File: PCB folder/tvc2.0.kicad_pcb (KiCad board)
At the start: 4 copper layers, 95 x 54 mm, 15 parts, among them U1 Teensy4.1, U5 LM7805_TO220

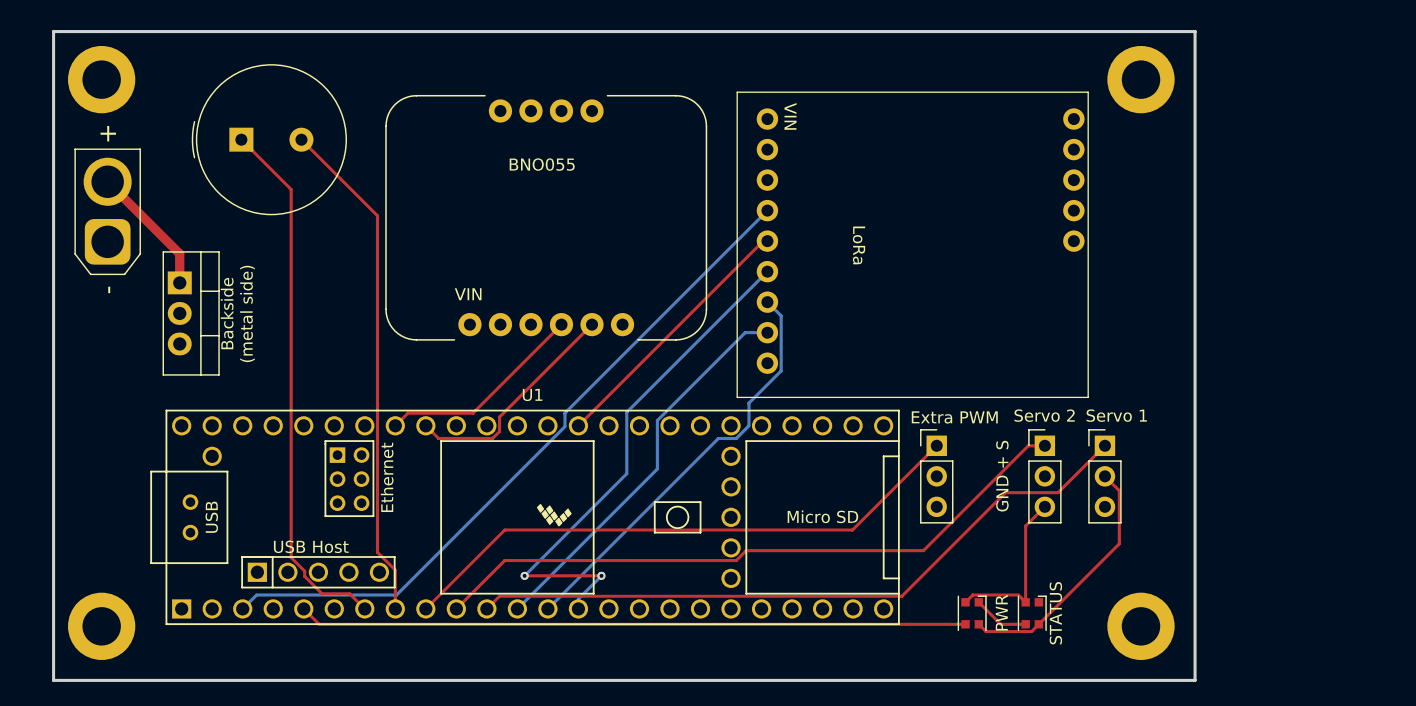
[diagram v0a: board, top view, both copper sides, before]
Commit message: funts: Added Pyro circuit in schematic
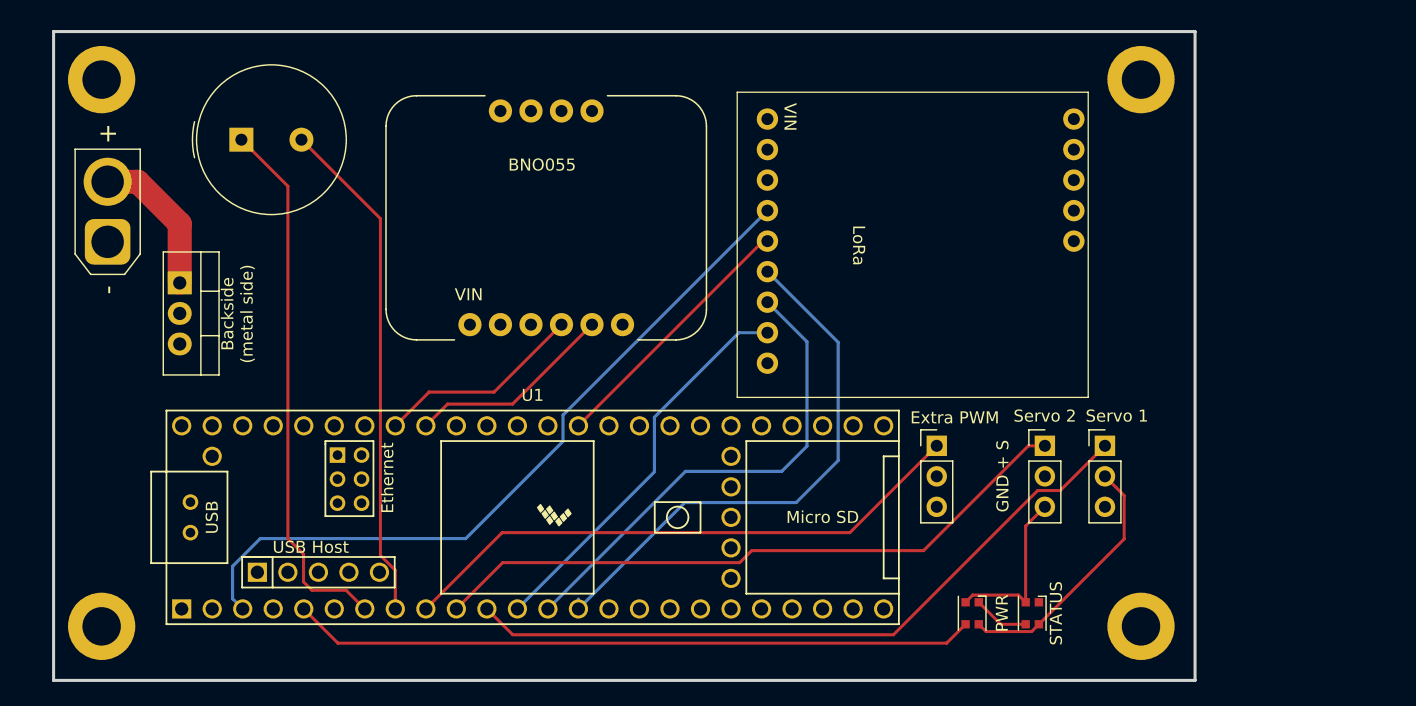
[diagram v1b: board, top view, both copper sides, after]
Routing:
- net /11_MOSI_CTX1: track 34.9 -> 40.5 mm
- net /1_TX1_CTX2_MISO1: track 58.1 -> 62.2 mm
- net /12_MISO_MQSL: track 43.6 -> 45.7 mm, vias 2 -> 0
- net /9_OUT1C: track 57.1 -> 58.8 mm
- net /18_A4_SDA: track 18.9 -> 17.3 mm
- net +7.5V: track 10.9 -> 12.4 mm
- net /3_LRCLK2: track 55.6 -> 56.9 mm

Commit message: functs: update PCB, add part excel
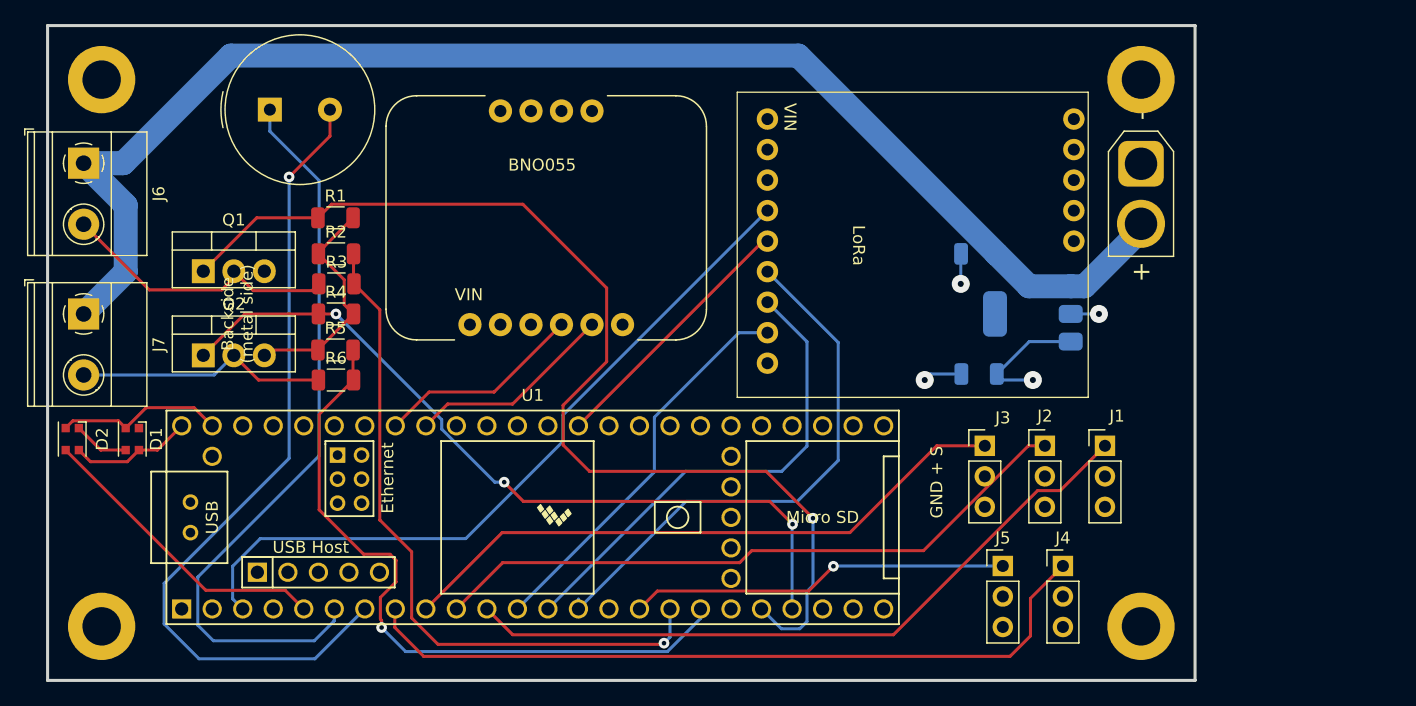
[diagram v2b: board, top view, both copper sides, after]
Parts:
- added C1: 0.33uf, Capacitor_SMD:C_1206_3216Metric, B.Cu at (202.5, 37.0)
- added C2: 0.1uf, Capacitor_SMD:C_1206_3216Metric, B.Cu at (202.5, 47.0)
- added J4: PWM Test OUT, Connector_PinHeader_2.54mm:PinHeader_1x03_P2.54mm_Vertical, F.Cu at (209.5, 63.0)
- added J5: PWM Test OUT, Connector_PinHeader_2.54mm:PinHeader_1x03_P2.54mm_Vertical, F.Cu at (204.5, 63.0)
- added J6: Screw_Terminal_01x02, TerminalBlock_Phoenix:TerminalBlock_Phoenix_MKDS-1,5-2-5.08_1x02_P5.08mm_Horizontal, F.Cu at (128.0, 29.5)
- added J7: Screw_Terminal_01x02, TerminalBlock_Phoenix:TerminalBlock_Phoenix_MKDS-1,5-2-5.08_1x02_P5.08mm_Horizontal, F.Cu at (128.0, 42.0)
- added Q1: IRLZ44NPBF, Package_TO_SOT_THT:TO-220-3_Vertical, F.Cu at (138.0, 38.4)
- added Q2: IRLZ44NPBF, Package_TO_SOT_THT:TO-220-3_Vertical, F.Cu at (138.0, 45.4)
- added R1: 1k, Resistor_SMD:R_1206_3216Metric, F.Cu at (149.0, 34.0)
- added R2: 51k, Resistor_SMD:R_1206_3216Metric, F.Cu at (149.0, 37.0)
- added R3: 91k, Resistor_SMD:R_1206_3216Metric, F.Cu at (149.0, 39.5)
- added R4: 1k, Resistor_SMD:R_1206_3216Metric, F.Cu at (149.0, 42.0)
- added R5: 51k, Resistor_SMD:R_1206_3216Metric, F.Cu at (149.0, 45.0)
- added R6: 91k, Resistor_SMD:R_1206_3216Metric, F.Cu at (149.0, 47.5)
- J1: renamed from Servo 1
- J2: renamed from Servo 2
- J3: renamed from Extra PWM
- U1: footprint Teensy4.1:Teensy41 -> tvc499:Teensy41
- U2: footprint LoRa_RF95:LoRa_RF95 Breakout -> tvc499:LoRa_RF95 Breakout
- U3: footprint BNO055:BNO055 -> tvc499:BNO055
- U5: footprint Package_TO_SOT_THT:TO-220-3_Vertical -> Package_TO_SOT_SMD:SOT-223; moved to B.Cu
- moved REF** 86.2 mm to (216.0, 29.5), turned to -90 degrees
- moved D2 76.3 mm to (127.0, 52.4)
- moved D1 76.3 mm to (132.1, 52.4)
- moved U5 71.0 mm to (207.0, 42.0), turned to 180 degrees
- moved J3 4.00 mm to (203.0, 53.0)
- moved BZ1 3.45 mm to (143.5, 25.0)
- renumbered STATUS to D1, PWR to D2
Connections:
- BZ1 pad 1: /5_IN2 -> /4_BCLK2
- BZ1 pad 2: /6_OUT1D -> /5_IN2
- U1 pad 46: (no net) -> +3.3V
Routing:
- net +7.5V: track 12.4 -> 117.6 mm
- net /28_RX7: track 0.00 -> 90.2 mm, vias 0 -> 1
- net /29_TX7: track 0.00 -> 65.2 mm, vias 0 -> 3
- net /4_BCLK2: track 0.00 -> 62.4 mm
- net /26_A12_MOSI1: track 0.00 -> 58.6 mm, vias 0 -> 1
- net /25_A11_RX6_SDA2: track 0.00 -> 57.3 mm, vias 0 -> 1
- net /24_A10_TX6_SCL2: track 0.00 -> 31.7 mm, vias 0 -> 1
- net /3_LRCLK2: track 56.9 -> 25.3 mm
- net GND: track 14.1 -> 41.4 mm, vias 0 -> 3
- net Net-(J6-Pin_2): track 0.00 -> 23.7 mm
- net /5_IN2: track 45.0 -> 68.6 mm, vias 0 -> 1
- net Net-(J7-Pin_2): track 0.00 -> 21.1 mm
- net /6_OUT1D: track 42.3 -> 63.1 mm
- net /7_RX2_OUT1A: track 48.1 -> 52.1 mm
- net +5V: track 21.4 -> 20.7 mm, vias 0 -> 1
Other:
- board size 95 x 54 mm -> 95.5 x 54.5 mm

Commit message: added pcb name date version
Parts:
- PWM 24: renamed from J5
- PWM 6: renamed from J4
- PWM 7: renamed from J3
- PWM 8: renamed from J2
- PWM 9: renamed from J1
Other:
- board text added: "C3C GRANT STEC TVC499 Flight Computer v1 11/20/24"
- board text added: "SERVO"
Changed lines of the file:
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@@
 		(descr "Through hole straight pin header, 1x03, 2.54mm pitch, single row")
 		(tags "Through hole pin header THT 1x03 2.54mm single row")
-		(property "Reference" "J3"
-			(at 1.5 -2.33 0)
+		(property "Reference" "PWM 7"
+			(at -0.8 -2.475 0)
 			(layer "F.SilkS")
 			(effects
@@
 		(descr "Through hole straight pin header, 1x03, 2.54mm pitch, single row")
 		(tags "Through hole pin header THT 1x03 2.54mm single row")
-		(property "Reference" "J2"
+		(property "Reference" "PWM 8"
 			(at 0 -2.475 0)
 			(layer "F.SilkS")
@@
 		(descr "Through hole straight pin header, 1x03, 2.54mm pitch, single row")
 		(tags "Through hole pin header THT 1x03 2.54mm single row")
-		(property "Reference" "J4"
-			(at 0 -2.33 0)
+		(property "Reference" "PWM 6"
+			(at 0.6 -2.375 0)
 			(layer "F.SilkS")
 			(effects
@@
 		(descr "Through hole straight pin header, 1x03, 2.54mm pitch, single row")
 		(tags "Through hole pin header THT 1x03 2.54mm single row")
-		(property "Reference" "J1"
-			(at 1 -2.475 0)
+		(property "Reference" "PWM 9"
+			(at 0.7 -2.475 0)
 			(layer "F.SilkS")
 			(effects
@@
 		(descr "Through hole straight pin header, 1x03, 2.54mm pitch, single row")
 		(tags "Through hole pin header THT 1x03 2.54mm single row")
-		(property "Reference" "J5"
+		(property "Reference" "PWM 24"
 			(at 0 -2.33 0)
 			(layer "F.SilkS")
@@
 		(property "Value" "PWM Test OUT"
 			(at 0 7.41 0)
-			(layer "F.Fab")
+			(layer "F.SilkS")
 			(effects
 				(font
@@
 	)
 	(gr_text "GND + S\n"
+		(at 200.7 65.6 90)
+		(layer "F.SilkS")
+		(effects
+			(font
+				(size 1 1)
+				(thickness 0.15)
+			)
+		)
+	)
+	(gr_text "SERVO\n"
+		(at 216 55.4 90)
+		(layer "F.SilkS")
+		(effects
+			(font
+				(size 1 1)
+				(thickness 0.15)
+			)
+		)
+	)
+	(gr_text "GND + S\n"
 		(at 199 56 90)
 		(layer "F.SilkS")
@@
 		(layer "F.SilkS")
 		(effects
+			(font
+				(size 1 1)
+				(thickness 0.15)
+			)
+		)
+	)
+	(gr_text "C3C GRANT STEC\nTVC499 \nFlight Computer v1 11/20/24"
+		(at 166.2 21 0)
+		(layer "F.SilkS")
+		(effects

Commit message: edit: final pcb files sent to JLC
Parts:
- added U4: ~, tvc499:BMP390, F.Cu at (228.0, 51.1)
- J1: renamed from PWM 9
- J2: renamed from PWM 8
- J3: renamed from PWM 7
- J4: renamed from PWM 6
- J5: renamed from PWM 24
- moved REF** 15.8 mm to (231.8, 68.0)
- moved REF** 15.8 mm to (231.8, 22.5)
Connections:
- U1 pad 46: +3.3V -> (no net)
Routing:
- net /16_A2_RX4_SCL1: track 0.00 -> 75.2 mm, vias 0 -> 1
- net /17_A3_TX4_SDA1: track 0.00 -> 72.4 mm, vias 0 -> 1
- net GND: track 41.4 -> 65.9 mm, vias 3 -> 0
- net +5V: track 20.7 -> 29.6 mm, vias 1 -> 0
- net Net-(J6-Pin_2): track 23.7 -> 26.9 mm
- net Net-(J7-Pin_2): track 21.1 -> 23.3 mm
- net /9_OUT1C: track 58.8 -> 61.0 mm
- net /8_TX2_IN1: track 54.6 -> 56.0 mm
- net +7.5V: track 117.6 -> 118.5 mm
- net /12_MISO_MQSL: track 45.7 -> 44.9 mm
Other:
- board size 95.5 x 54.5 mm -> 111.8 x 54.5 mm
- board text added: "BMP390"
- board text added: "GND"
- board text removed: "Backside (metal side)"
